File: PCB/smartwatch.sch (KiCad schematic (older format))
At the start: 55 parts, among them U1 STM32F103C8T6, U2 HM-10, U3 M25P40, U4 BMC150, U5 BMP180, U6 STC4054, U7 NCP551, U8 UG-2864HSWEG01, X1 PLS1, X2 PLS1, X3 PLS1, X4 PLS1, X5 PLS1, X6 PLS1

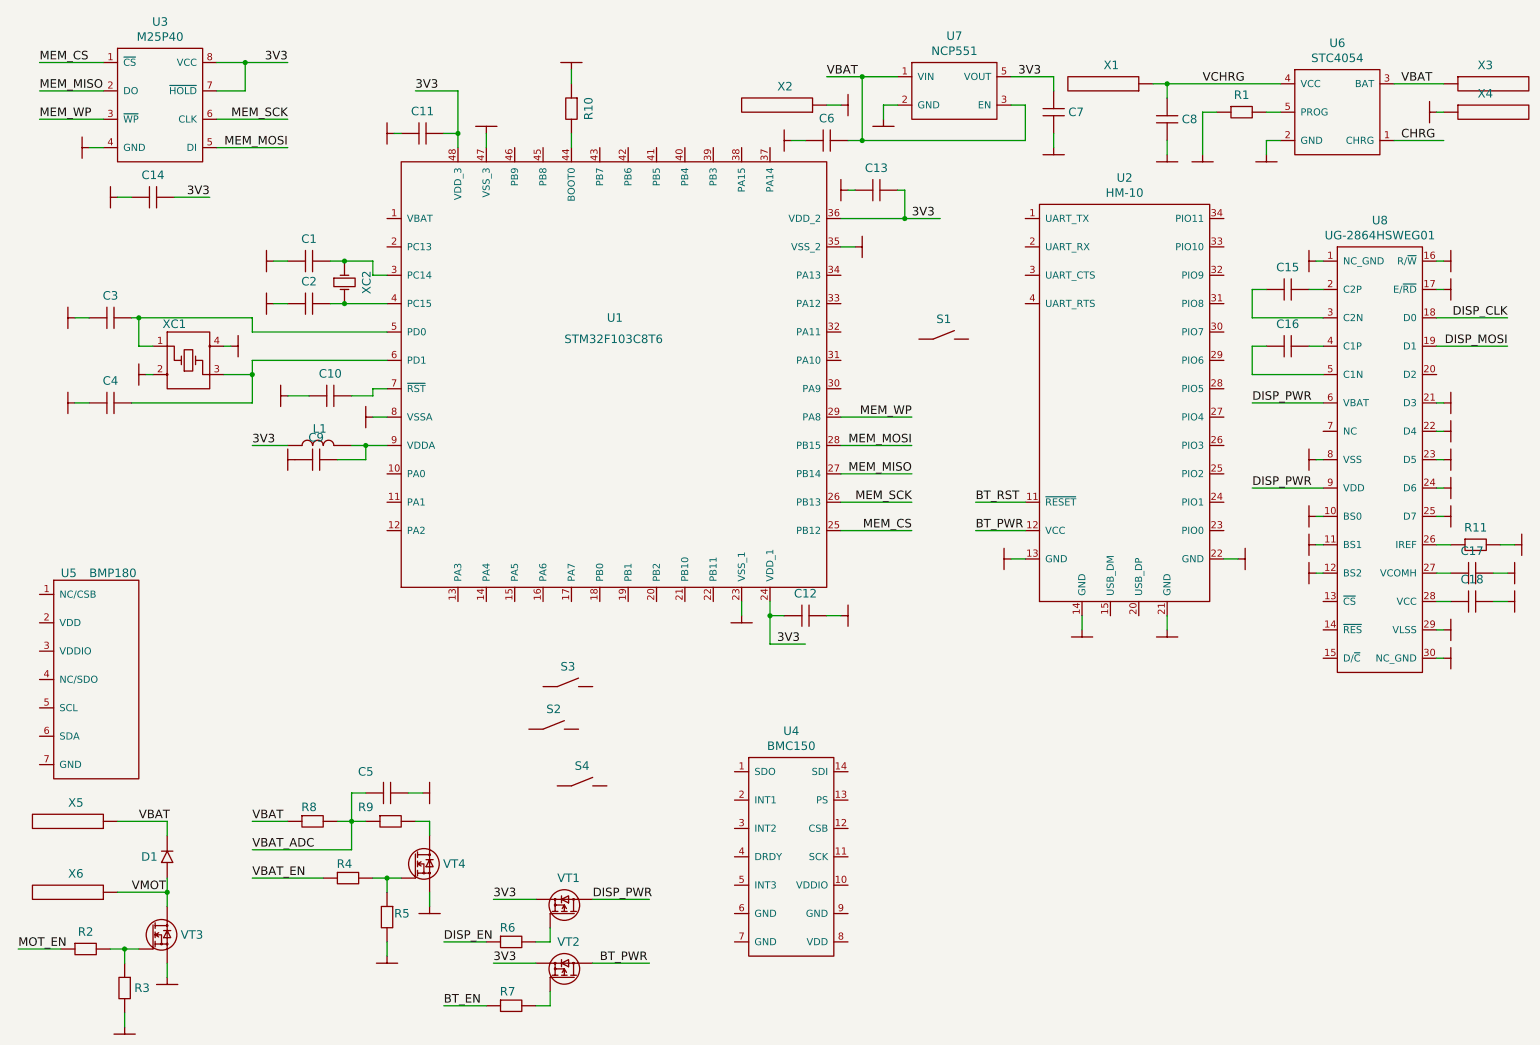
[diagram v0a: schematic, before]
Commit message: First iteration (only SH1106 and some GUI classes work fine)
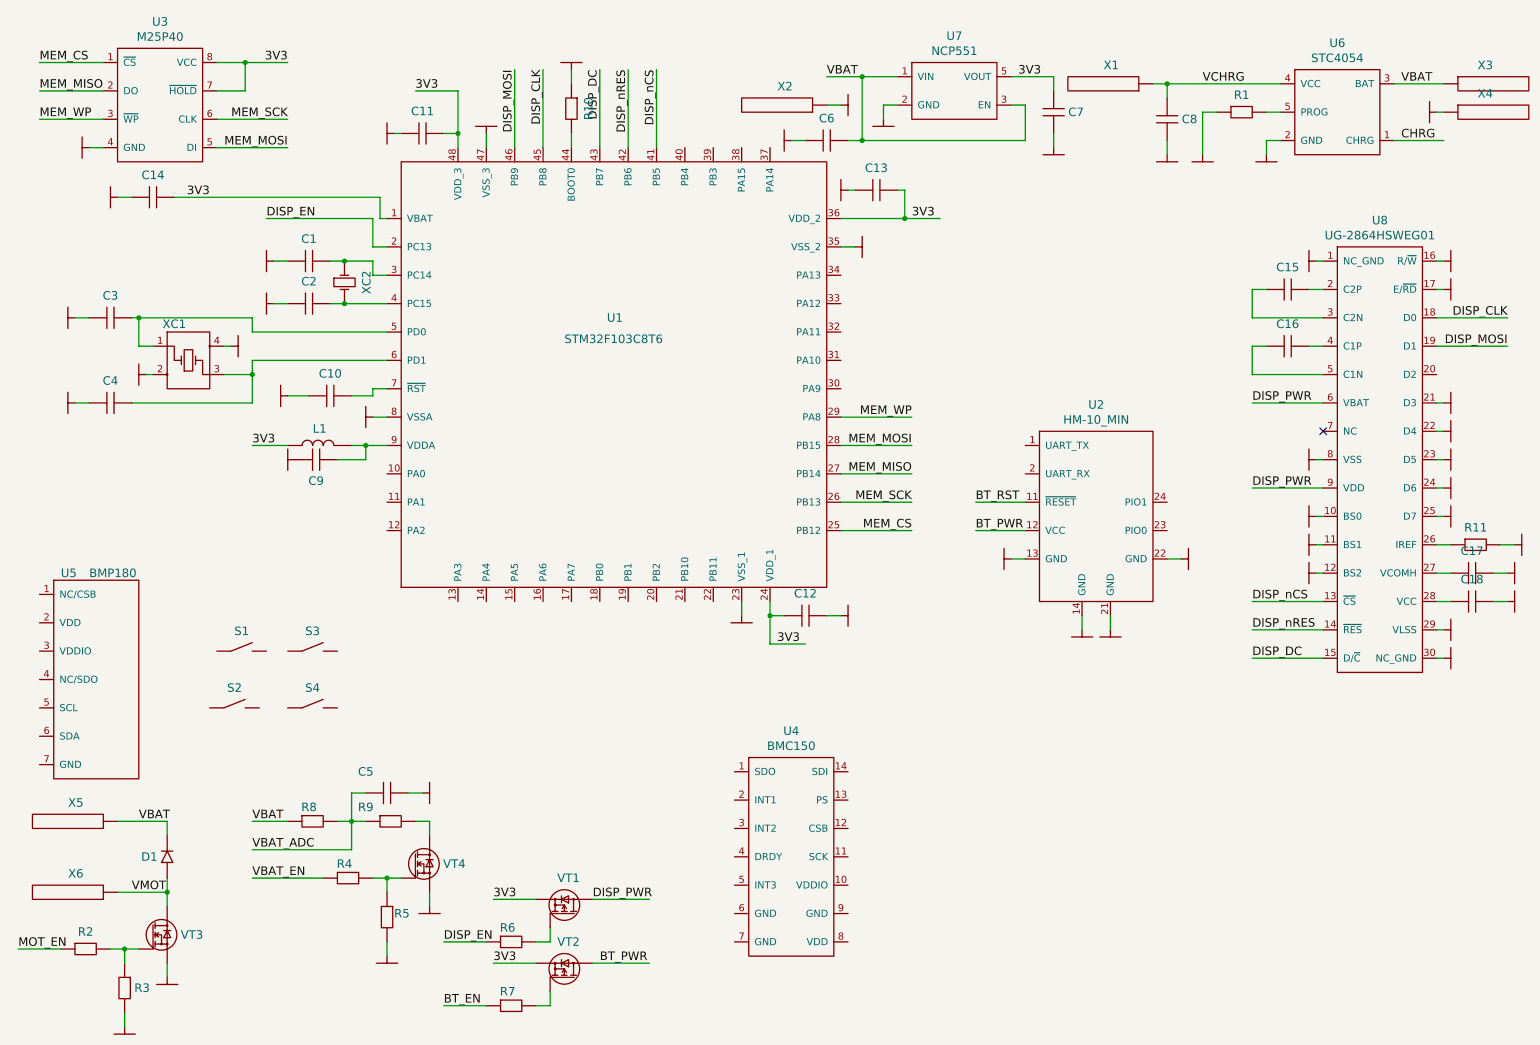
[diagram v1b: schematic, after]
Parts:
- removed U2: HM-10, MODULES:HM-10, symbol HM-10
- added U2: HM-10_MIN, MODULES:HM-10_MIN, symbol HM-10_MIN
- C15, C16, C17, C18: value capacitor -> 1u/10V
- R11: value resistor -> 390k
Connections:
- net 3V3: now also U1.1 (VBAT)
- net BT_PWR: now also U2.12 (VCC)
- net BT_RST: now also U2.11 (~RESET)
- net DISP_CLK: now also U1.45 (PB8)
- net DISP_EN: now also U1.2 (PC13)
- net DISP_MOSI: now also U1.46 (PB9)
- net GND: now also U2.13 (GND), U2.14 (GND), U2.21 (GND), U2.22 (GND)
- net DISP_nCS: now reaches U1.41 (PB5)
- net DISP_nCS: now also U8.13 (~CS)
- net DISP_nRES: now reaches U1.42 (PB6)
- net DISP_nRES: now also U8.14 (~RES)
- net DISP_DC: now reaches U1.43 (PB7)
- net DISP_DC: now also U8.15 (D/~C)
- no-connect marks 0 -> 1
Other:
- moved on the sheet: S1, S2, S3, S4
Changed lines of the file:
@@
 L button_NO S1
 U 1 1 56FFF456
-P 6950 2800
-F 0 "S1" H 7125 2941 60  0000 C CNN
-F 1 "button_NO" H 7100 2700 60  0001 C CNN
-F 2 "BUTTONS:B3U3000P" H 6950 2800 60  0001 C CNN
-F 3 "" H 6950 2800 60  0000 C CNN
-	1    6950 2800
+P 2000 5000
+F 0 "S1" H 2175 5141 60  0000 C CNN
+F 1 "button_NO" H 2150 4900 60  0001 C CNN
+F 2 "BUTTONS:B3U3000P" H 2000 5000 60  0001 C CNN
+F 3 "" H 2000 5000 60  0000 C CNN
+	1    2000 5000
 	1    0    0    -1
 $EndComp
@@
 $EndComp
 $Comp
-L HM-10 U2
-U 1 1 570014EF
-P 7700 3150
-F 0 "U2" H 8400 4637 60  0000 C CNN
-F 1 "HM-10" H 8400 4531 60  0000 C CNN
-F 2 "MODULES:HM-10" H 7700 4350 60  0001 C CNN
-F 3 "" H 7700 4350 60  0000 C CNN
-	1    7700 3150
-	1    0    0    -1
-$EndComp
-$Comp
 L button_NO S3
 U 1 1 57001663
-P 4300 5250
-F 0 "S3" H 4475 5391 60  0000 C CNN
-F 1 "button_NO" H 4450 5150 60  0001 C CNN
-F 2 "BUTTONS:B3U3000P" H 4300 5250 60  0001 C CNN
-F 3 "" H 4300 5250 60  0000 C CNN
-	1    4300 5250
+P 2500 5000
+F 0 "S3" H 2675 5141 60  0000 C CNN
+F 1 "button_NO" H 2650 4900 60  0001 C CNN
+F 2 "BUTTONS:B3U3000P" H 2500 5000 60  0001 C CNN
+F 3 "" H 2500 5000 60  0000 C CNN
+	1    2500 5000
 	1    0    0    -1
 $EndComp
@@
 L button_NO S2
 U 1 1 570016B7
-P 4200 5550
-F 0 "S2" H 4375 5691 60  0000 C CNN
-F 1 "button_NO" H 4350 5450 60  0001 C CNN
-F 2 "BUTTONS:B3U3000P" H 4200 5550 60  0001 C CNN
-F 3 "" H 4200 5550 60  0000 C CNN
-	1    4200 5550
+P 1950 5400
+F 0 "S2" H 2125 5541 60  0000 C CNN
+F 1 "button_NO" H 2100 5300 60  0001 C CNN
+F 2 "BUTTONS:B3U3000P" H 1950 5400 60  0001 C CNN
+F 3 "" H 1950 5400 60  0000 C CNN
+	1    1950 5400
 	1    0    0    -1
 $EndComp
@@
 L button_NO S4
 U 1 1 570016F5
-P 4400 5950
-F 0 "S4" H 4575 6091 60  0000 C CNN
-F 1 "button_NO" H 4550 5850 60  0001 C CNN
-F 2 "BUTTONS:B3U3000P" H 4400 5950 60  0001 C CNN
-F 3 "" H 4400 5950 60  0000 C CNN
-	1    4400 5950
+P 2500 5400
+F 0 "S4" H 2675 5541 60  0000 C CNN
+F 1 "button_NO" H 2650 5300 60  0001 C CNN
+F 2 "BUTTONS:B3U3000P" H 2500 5400 60  0001 C CNN
+F 3 "" H 2500 5400 60  0000 C CNN
+	1    2500 5400
 	1    0    0    -1
 $EndComp
@@
 U 1 1 57061B34
 P 2550 3650
-F 0 "C9" H 2700 3806 60  0000 C CNN
+F 0 "C9" H 2700 3500 60  0000 C CNN
 F 1 "capacitor" H 2700 3550 60  0001 C CNN
 F 2 "discrete_SMD:0402_C" H 2550 3650 60  0001 C CNN
@@
 L GND #PWR028
 U 1 1 57067456
-P 8700 4850
-F 0 "#PWR028" H 8700 4700 50  0001 C CNN
-F 1 "GND" H 8700 4750 50  0001 C CNN
-F 2 "" H 8700 4850 60  0000 C CNN
-F 3 "" H 8700 4850 60  0000 C CNN
-	1    8700 4850
+P 8300 4850
+F 0 "#PWR028" H 8300 4700 50  0001 C CNN
+F 1 "GND" H 8300 4750 50  0001 C CNN
+F 2 "" H 8300 4850 60  0000 C CNN
+F 3 "" H 8300 4850 60  0000 C CNN
+	1    8300 4850
 	1    0    0    -1
 $EndComp
@@
 L GND #PWR029
 U 1 1 570674EE
-P 9200 4350
-F 0 "#PWR029" H 9200 4200 50  0001 C CNN
-F 1 "GND" H 9200 4250 50  0001 C CNN
-F 2 "" H 9200 4350 60  0000 C CNN
-F 3 "" H 9200 4350 60  0000 C CNN
-	1    9200 4350
+P 8800 4350
+F 0 "#PWR029" H 8800 4200 50  0001 C CNN
+F 1 "GND" H 8800 4250 50  0001 C CNN
+F 2 "" H 8800 4350 60  0000 C CNN
+F 3 "" H 8800 4350 60  0000 C CNN
+	1    8800 4350
 	0    -1   -1   0
 $EndComp
 Wire Wire Line
 	8100 4850 8100 4750
-Wire Wire Line
-	8700 4850 8700 4750
 Wire Wire Line
 	7600 4350 7700 4350
@@
 3V3
 Wire Wire Line
-	1950 1800 1700 1800
+	1700 1800 3150 1800
 Wire Wire Line
 	1300 1800 1400 1800
@@
 P 9400 2450
 F 0 "C15" H 9550 2606 60  0000 C CNN
-F 1 "capacitor" H 9550 2350 60  0001 C CNN
+F 1 "1u/10V" H 9550 2350 60  0001 C CNN
 F 2 "discrete_SMD:0603_C" H 9400 2450 60  0001 C CNN
 F 3 "" H 9400 2450 60  0000 C CNN
@@
 P 9400 2850
 F 0 "C16" H 9550 3006 60  0000 C CNN
-F 1 "capacitor" H 9550 2750 60  0001 C CNN
+F 1 "1u/10V" H 9550 2750 60  0001 C CNN
 F 2 "discrete_SMD:0603_C" H 9400 2850 60  0001 C CNN
 F 3 "" H 9400 2850 60  0000 C CNN
@@
 P 10700 4250
 F 0 "R11" H 10875 4371 60  0000 C CNN
-F 1 "resistor" H 10850 4150 60  0001 C CNN
+F 1 "390k" H 10850 4150 60  0001 C CNN
 F 2 "discrete_SMD:0402_R" H 10700 4250 60  0001 C CNN
 F 3 "" H 10700 4250 60  0000 C CNN
@@
 $EndComp
 Wire Wire Line
-	9100 4350 9200 4350
+	8700 4350 8800 4350
 $Comp
 L GND #PWR036
@@
 P 10700 4450
 F 0 "C17" H 10850 4606 60  0000 C CNN
-F 1 "capacitor" H 10850 4350 60  0001 C CNN
+F 1 "1u/10V" H 10850 4350 60  0001 C CNN
 F 2 "discrete_SMD:0603_C" H 10700 4450 60  0001 C CNN
 F 3 "" H 10700 4450 60  0000 C CNN
@@
 P 10700 4650
 F 0 "C18" H 10850 4806 60  0000 C CNN
-F 1 "capacitor" H 10850 4550 60  0001 C CNN
+F 1 "1u/10V" H 10850 4550 60  0001 C CNN
 F 2 "discrete_SMD:0603_C" H 10700 4650 60  0001 C CNN
 F 3 "" H 10700 4650 60  0000 C CNN
@@
 Wire Wire Line
 	11100 2850 10600 2850
+Text Label 9300 4650 0    60   ~ 0
+DISP_nCS
+Text Label 9300 4850 0    60   ~ 0
+DISP_nRES
+Text Label 9300 5050 0    60   ~ 0
+DISP_DC
+Wire Wire Line
+	9300 4650 9800 4650
+Wire Wire Line
+	9300 4850 9800 4850
+Wire Wire Line
+	9300 5050 9800 5050
+NoConn ~ 9800 3450
+Text Label 2350 1950 0    60   ~ 0
+DISP_EN
+Wire Wire Line
+	2350 1950 3100 1950
+Wire Wire Line
+	3100 1950 3100 2150
+Wire Wire Line
+	3100 2150 3200 2150
+Wire Wire Line
+	3200 1950 3150 1950
+Wire Wire Line
+	3150 1950 3150 1800
+Text Label 4100 900  3    60   ~ 0
+DISP_MOSI
+Text Label 4300 900  3    60   ~ 0
+DISP_CLK
+Text Label 4700 900  3    60   ~ 0
+DISP_DC
+Text Label 4900 900  3    60   ~ 0
+DISP_nRES
+Text Label 5100 900  3    60   ~ 0
+DISP_nCS
+Wire Wire Line
+	4100 900  4100 1450
+Wire Wire Line
+	4300 900  4300 1450
+Wire Wire Line
+	4700 900  4700 1450
+Wire Wire Line
+	4900 900  4900 1450
+Wire Wire Line
+	5100 900  5100 1450
+$Comp
+L HM-10_MIN U2
+U 1 1 571683E7
+P 7700 3550
+F 0 "U2" H 8200 3837 60  0000 C CNN
+F 1 "HM-10_MIN" H 8200 3731 60  0000 C CNN
+F 2 "MODULES:HM-10_MIN" H 7700 3550 60  0001 C CNN
+F 3 "" H 7700 3550 60  0000 C CNN
+	1    7700 3550
+	1    0    0    -1
+$EndComp
+Wire Wire Line
+	8300 4850 8300 4750
 $EndSCHEMATC

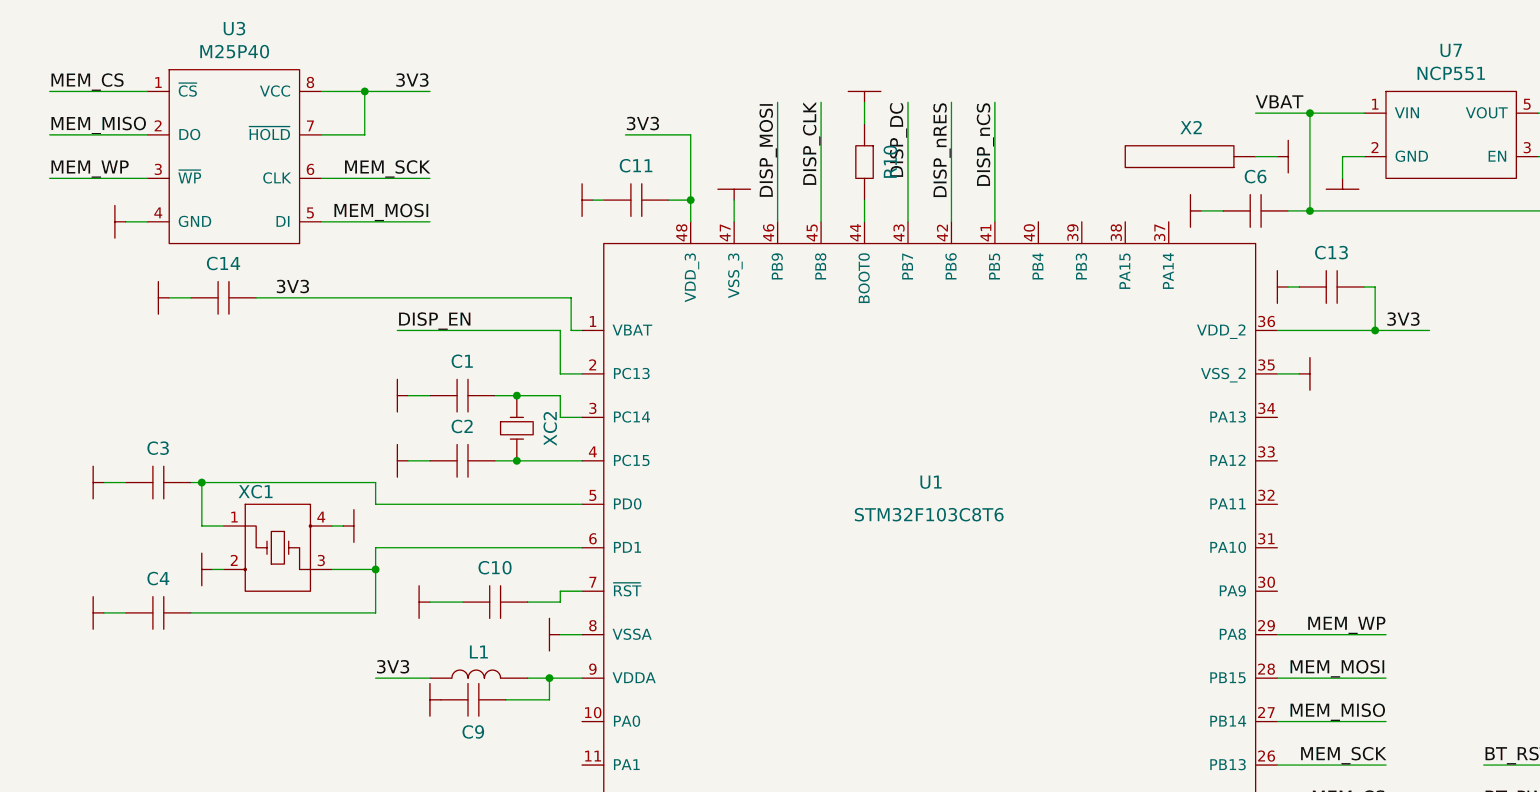
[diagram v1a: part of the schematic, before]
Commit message: SPI Flash nWR is connected to 3V3
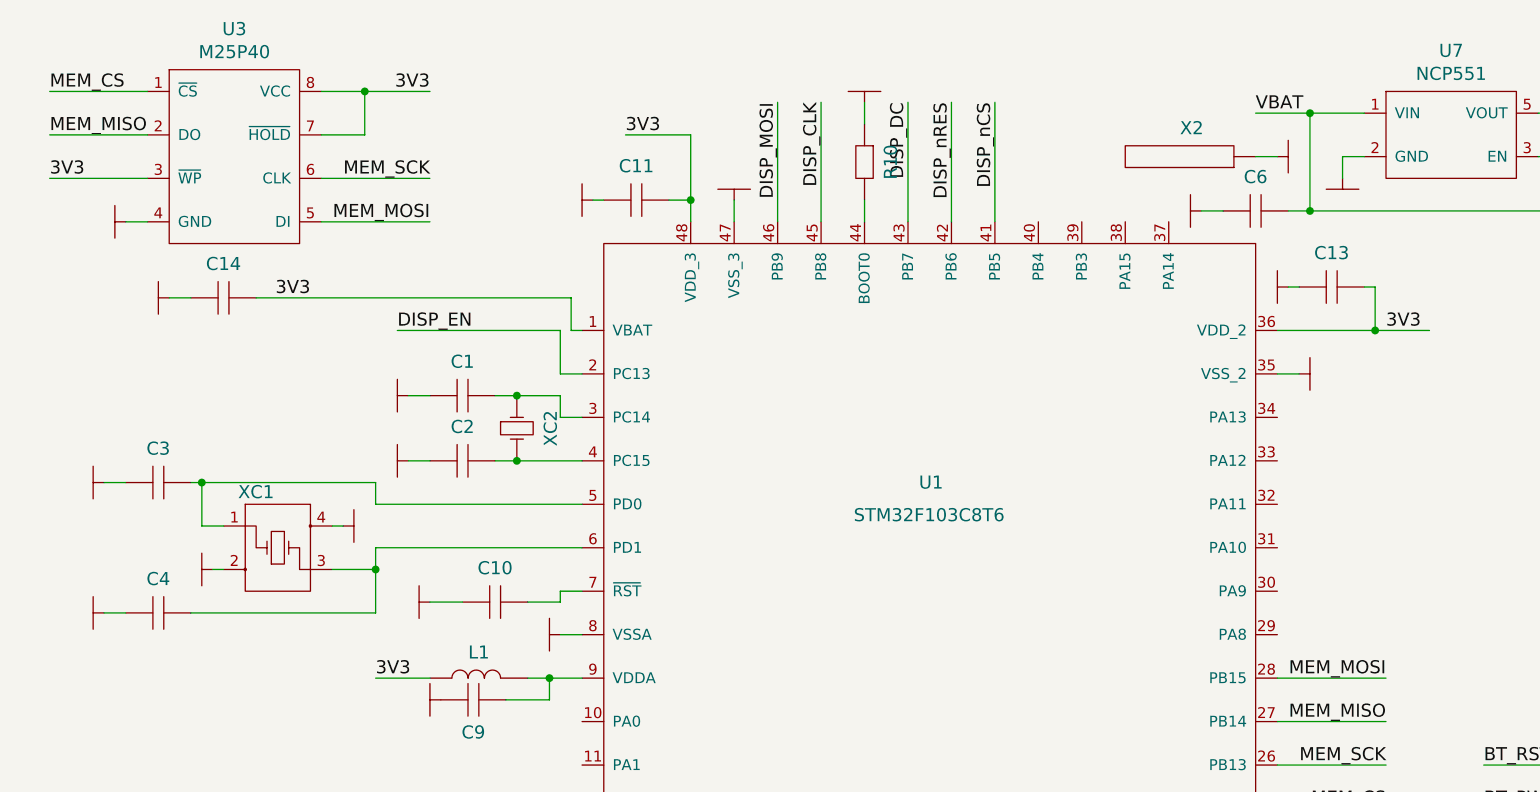
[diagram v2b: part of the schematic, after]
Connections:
- net 3V3: now also U3.3 (~WP)
- net MEM_WP: no longer names the net of U1.29 (PA8)
- net MEM_WP: no longer U3.3 (~WP)
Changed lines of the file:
@@
 Text Label 750  850  0    60   ~ 0
 MEM_CS
-Text Label 6900 3350 2    60   ~ 0
-MEM_WP
-Text Label 750  1250 0    60   ~ 0
-MEM_WP
-Wire Wire Line
-	6900 3350 6400 3350
 Wire Wire Line
 	6900 3550 6400 3550
@@
 Wire Wire Line
 	8300 4850 8300 4750
+Text Label 750  1250 0    60   ~ 0
+3V3
 $EndSCHEMATC

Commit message: PCB (everything is done, should be checked)
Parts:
- added C20: capacitor, discrete_SMD:0402_C, symbol capacitor
- added LG?1: LOGO, LOGO:OSHW, symbol LOGO
- added R12, R13: resistor, discrete_SMD:0402_R, symbol resistor
- added R14, R15: 390k, discrete_SMD:0402_R, symbol resistor
- added VT5: MOSFET_P_DGS, IR:PQFN2x2, symbol MOSFET_P_DGS
- added X10: 3V3, CONNECTORS:SLD_POINT, symbol PLS1
- added X7: SWCLK, CONNECTORS:SLD_POINT, symbol PLS1
- added X8: SWDIO, CONNECTORS:SLD_POINT, symbol PLS1
- added X9: GND, CONNECTORS:SLD_POINT, symbol PLS1
- U8: value UG-2864HSWEG01 -> SH1106
- X1: value PLS1 -> VCHRG
- X2, X4: value PLS1 -> GND
- X3, X5: value PLS1 -> VBAT
- X6: value PLS1 -> VMOT
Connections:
- net 3V3: now also U4.10 (VDDIO), U4.12 (CSB), U4.13 (PS), U4.8 (VDD), U5.2 (VDD), U5.3 (VDDIO), C20.2, R12.1, R13.1, X10.1
- net BT_EN: now also U1.40 (PB4)
- net CHRG: now also U1.38 (PA15)
- net GND: now also C5.1, R9.1, S1.2, S2.1, S3.2, S4.1, U4.1 (SDO), U4.6 (GND), U4.7 (GND), U4.9 (GND), U5.7 (GND), C20.1, X9.1; no longer C5.2, R5.2
- net MOT_EN: now also U1.29 (PA8)
- net VBAT: now also R5.1, VT5.3 (S); no longer R8.1
- net VBAT_ADC: now also C5.2, R8.1, R9.2, U1.10 (PA0); no longer C5.1, R8.2, R9.1
- net VBAT_EN: now also U1.12 (PA2)
- net VDDA: now reaches C9.2, L1.2, U1.9 (VDDA)
- net S3: now reaches U1.11 (PA1)
- net S3: now also S3.1
- net BT_STATE: now reaches U1.13 (PA3)
- net BT_STATE: now also U2.24 (PIO1)
- net S4: now reaches U1.16 (PA6)
- net S4: now also S4.2
- net ACC_IRQ3: now reaches U1.17 (PA7)
- net ACC_IRQ3: now also U4.5 (INT3)
- net ACC_DRDY: now reaches U1.18 (PB0)
- net ACC_DRDY: now also U4.4 (DRDY)
- net ACC_IRQ2: now reaches U1.19 (PB1)
- net ACC_IRQ2: now also U4.3 (INT2)
- net ACC_IRQ1: now reaches U1.20 (PB2)
- net ACC_IRQ1: now also U4.2 (INT1)
- net I2C_SCL: now reaches U1.21 (PB10)
- net I2C_SCL: now also U4.11 (SCK), U5.5 (SCL), R13.2
- net I2C_SDA: now reaches U1.22 (PB11)
- net I2C_SDA: now also U4.14 (SDI), U5.6 (SDA), R12.2
- net BT_TX: now reaches U1.30 (PA9)
- net BT_TX: now also R15.1
- net BT_RX: now reaches U1.31 (PA10)
- net BT_RX: now also R14.1
- net S1: now reaches U1.33 (PA12)
- net S1: now also S1.1
- net SWDIO: now reaches U1.34 (PA13)
- net SWDIO: now also X8.1
- net SWCLK: now reaches U1.37 (PA14)
- net SWCLK: now also X7.1
- net S2: now reaches U1.39 (PB3)
- net S2: now also S2.2
- net at VT4.1 (D): now also R5.2, VT5.2 (G); no longer R9.2
- net at R4.2, VT4.2 (G): no longer R5.1
- net at U2.1 (UART_TX): now also R14.2
- net at U2.2 (UART_RX): now also R15.2
- net BT_RST: no longer names the net of U2.11 (~RESET)
- new net: R8.2, VT5.1 (D)
- no-connect marks 1 -> 9
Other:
- moved on the sheet: C1, C10, C11, C12, C13, C14, C15, C16, C17, C18, C2, C3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
